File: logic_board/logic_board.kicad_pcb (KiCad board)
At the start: 4 copper layers, 80 x 30 mm, 61 parts, among them J1 SWD, J2 Audio In, J3 SJ2-3595X-SMT, J4 Amphenol 124015, J5 Batt, J6 Serial, SW1 TL3315NF160Q, SW2 TL3315NF160Q, SW3 TL3315NF160Q, SW4 TL3315NF160Q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

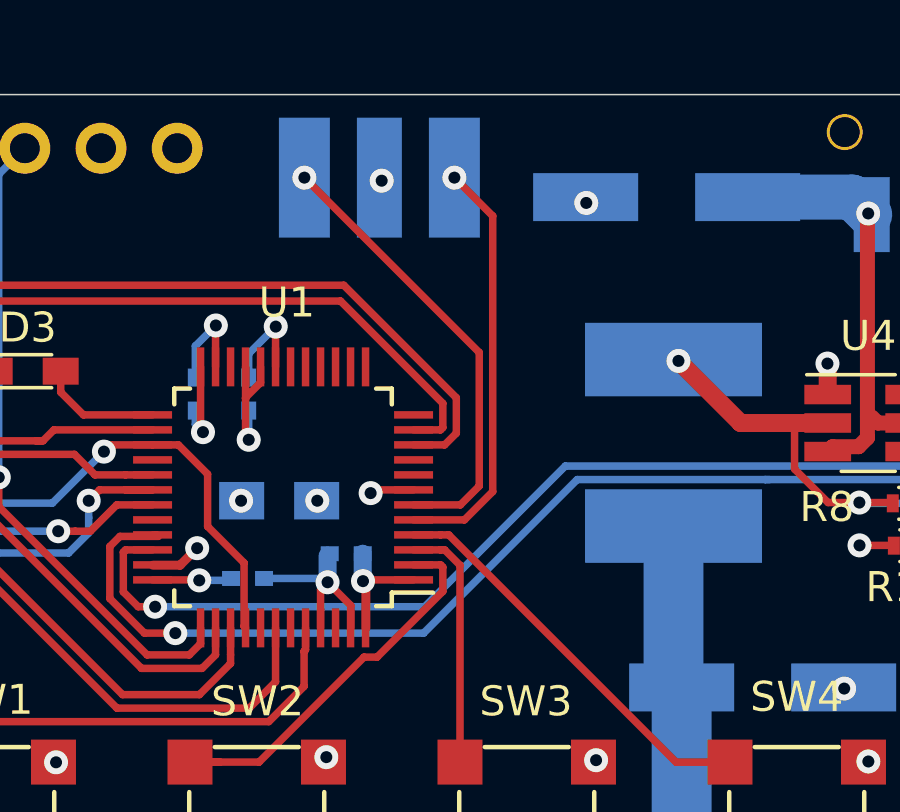
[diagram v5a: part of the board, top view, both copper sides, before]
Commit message: Move resonator closer to MCU.
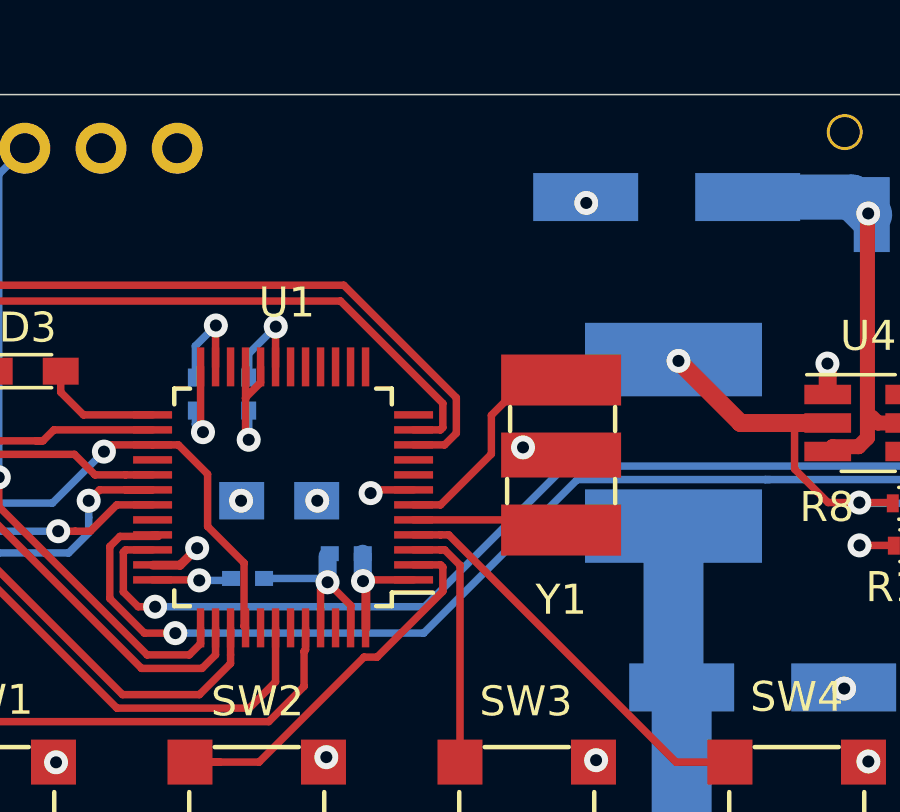
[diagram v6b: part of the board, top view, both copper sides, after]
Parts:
- Y1: moved to F.Cu
- moved Y1 11.1 mm to (152.1, 112.0), turned to 270 degrees
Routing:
- net Net-(U1-Pad5): track 14.0 -> 5.06 mm, vias 1 -> 0
- net Net-(U1-Pad6): track 15.1 -> 7.40 mm, vias 1 -> 0
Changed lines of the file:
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@@
     (thickness 1.6)
     (drawings 21)
-    (tracks 553)
+    (tracks 550)
     (zones 0)
     (modules 61)
@@
       (net 51 "Net-(U3-Pad26)"))
   )
-  (module custom_footprints:AWSCR-8.00CPLB-C30-T4 (layer B.Cu)
-    (at 146.0881 102.7684)
-    (fp_text reference Y1 (at -0.0381 3.6576) (layer B.SilkS)
-      (effects (font (size 1 1) (thickness 0.15)) (justify mirror))
-    )
-    (fp_text value "8 MHz" (at 1 5.6) (layer B.Fab)
-      (effects (font (size 1 1) (thickness 0.15)) (justify mirror))
-    )
-    (fp_line (start 0.8 -1.8) (end 1.6 -1.8) (layer B.SilkS) (width 0.15))
-    (fp_line (start 0.8 1.8) (end 1.6 1.8) (layer B.SilkS) (width 0.15))
-    (fp_line (start -0.8 -1.7) (end -1.6 -1.7) (layer B.SilkS) (width 0.15))
-    (fp_line (start -1.6 1.8) (end -0.8 1.8) (layer B.SilkS) (width 0.15))
-    (fp_line (start -4.2 -2.5) (end -4.2 2.5) (layer B.CrtYd) (width 0.12))
-    (fp_line (start -4.2 -2.5) (end 4.2 -2.5) (layer B.CrtYd) (width 0.12))
-    (fp_line (start 4.2 2.5) (end 4.2 -2.5) (layer B.CrtYd) (width 0.12))
-    (fp_line (start -4.2 2.5) (end 4.2 2.5) (layer B.CrtYd) (width 0.12))
-    (pad 3 smd rect (at 2.5 0) (size 1.7 4) (layers B.Cu B.Paste B.Mask)
+  (module custom_footprints:AWSCR-8.00CPLB-C30-T4 (layer F.Cu)
+    (at 152.146 112.014 270)
+    (fp_text reference Y1 (at 4.826 0) (layer F.SilkS)
+      (effects (font (size 1 1) (thickness 0.15)))
+    )
+    (fp_text value "8 MHz" (at 1 -5.6 270) (layer F.Fab)
+      (effects (font (size 1 1) (thickness 0.15)))
+    )
+    (fp_line (start 0.8 1.8) (end 1.6 1.8) (layer F.SilkS) (width 0.15))
+    (fp_line (start 0.8 -1.8) (end 1.6 -1.8) (layer F.SilkS) (width 0.15))
+    (fp_line (start -0.8 1.7) (end -1.6 1.7) (layer F.SilkS) (width 0.15))
+    (fp_line (start -1.6 -1.8) (end -0.8 -1.8) (layer F.SilkS) (width 0.15))
+    (fp_line (start -4.2 2.5) (end -4.2 -2.5) (layer F.CrtYd) (width 0.12))
+    (fp_line (start -4.2 2.5) (end 4.2 2.5) (layer F.CrtYd) (width 0.12))
+    (fp_line (start 4.2 -2.5) (end 4.2 2.5) (layer F.CrtYd) (width 0.12))
+    (fp_line (start -4.2 -2.5) (end 4.2 -2.5) (layer F.CrtYd) (width 0.12))
+    (pad 3 smd rect (at 2.5 0 270) (size 1.7 4) (layers F.Cu F.Paste F.Mask)
       (net 32 "Net-(U1-Pad5)"))
-    (pad 2 smd rect (at 0 0) (size 1.5 4) (layers B.Cu B.Paste B.Mask)
-      (net 2 GND))
-    (pad 1 smd rect (at -2.5 0) (size 1.7 4) (layers B.Cu B.Paste B.Mask)
+    (pad 2 smd rect (at 0 0 270) (size 1.5 4) (layers F.Cu F.Paste F.Mask)
+      (net 2 GND))
+    (pad 1 smd rect (at -2.5 0 270) (size 1.7 4) (layers F.Cu F.Paste F.Mask)
       (net 33 "Net-(U1-Pad6)"))
   )
@@
   (gr_line (start 180 102.5) (end 180 127.5) (layer Edge.Cuts) (width 0.05))
   (gr_line (start 102.5 100) (end 113 100) (layer Edge.Cuts) (width 0.05))
+  (via (at 150.876 111.76) (size 0.8) (drill 0.4) (layers F.Cu B.Cu) (net 2))
   (via (at 141.478 113.538) (size 0.8) (drill 0.4) (layers F.Cu B.Cu) (net 1))
   (via (at 156.17952 126.73076) (size 0.8) (drill 0.4) (layers F.Cu B.Cu) (net 1))
@@
   (via (at 166.37 128.7145) (size 0.8) (drill 0.4) (layers F.Cu B.Cu) (net 2))
   (via (at 152.9842 103.61168) (size 0.8) (drill 0.4) (layers F.Cu B.Cu) (net 2))
-  (via (at 146.1643 102.87) (size 0.8) (drill 0.4) (layers F.Cu B.Cu) (net 2))
   (via (at 160.6169 126.5301) (size 0.8) (drill 0.4) (layers F.Cu B.Cu) (net 2))
   (via (at 161.5821 119.7991) (size 0.8) (drill 0.4) (layers F.Cu B.Cu) (net 2))
@@
   (segment (start 172.7835 128.3407) (end 172.7907 128.3335) (width 0.25) (layer F.Cu) (net 31))
   (segment (start 172.7835 129.3114) (end 172.7835 128.3407) (width 0.25) (layer F.Cu) (net 31))
-  (via (at 148.5881 102.7684) (size 0.8) (drill 0.4) (layers F.Cu B.Cu) (net 32))
-  (segment (start 149.866611 104.046911) (end 148.5881 102.7684) (width 0.25) (layer F.Cu) (net 32))
-  (segment (start 149.866611 113.234201) (end 149.866611 104.046911) (width 0.25) (layer F.Cu) (net 32))
-  (segment (start 148.924572 114.17624) (end 149.866611 113.234201) (width 0.25) (layer F.Cu) (net 32))
-  (segment (start 147.22754 114.17624) (end 148.924572 114.17624) (width 0.25) (layer F.Cu) (net 32))
-  (segment (start 149.416601 108.596901) (end 143.5881 102.7684) (width 0.25) (layer F.Cu) (net 33))
-  (via (at 143.5881 102.7684) (size 0.8) (drill 0.4) (layers F.Cu B.Cu) (net 33))
-  (segment (start 148.788162 113.67624) (end 149.416601 113.047801) (width 0.25) (layer F.Cu) (net 33))
-  (segment (start 149.416601 113.047801) (end 149.416601 108.596901) (width 0.25) (layer F.Cu) (net 33))
-  (segment (start 147.22754 113.67624) (end 148.788162 113.67624) (width 0.25) (layer F.Cu) (net 33))
+  (segment (start 151.80824 114.17624) (end 152.146 114.514) (width 0.25) (layer F.Cu) (net 32))
+  (segment (start 147.22754 114.17624) (end 151.80824 114.17624) (width 0.25) (layer F.Cu) (net 32))
+  (segment (start 150.996 109.514) (end 152.146 109.514) (width 0.25) (layer F.Cu) (net 33))
+  (segment (start 149.820999 110.689001) (end 150.996 109.514) (width 0.25) (layer F.Cu) (net 33))
+  (segment (start 149.820999 111.982781) (end 149.820999 110.689001) (width 0.25) (layer F.Cu) (net 33))
+  (segment (start 148.12754 113.67624) (end 149.820999 111.982781) (width 0.25) (layer F.Cu) (net 33))
+  (segment (start 147.22754 113.67624) (end 148.12754 113.67624) (width 0.25) (layer F.Cu) (net 33))
   (segment (start 114.398372 117.387396) (end 120.24406 111.54171) (width 0.25) (layer F.Cu) (net 40))
   (segment (start 114.398371 120.906571) (end 114.398372 117.387396) (width 0.25) (layer F.Cu) (net 40))

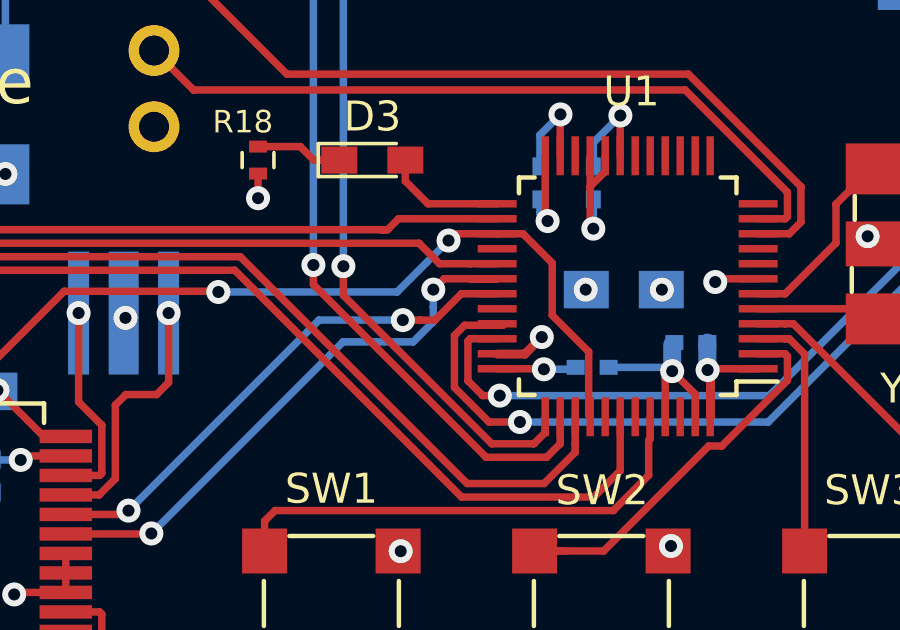
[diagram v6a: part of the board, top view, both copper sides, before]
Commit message: Move I2C2_SDA from PA8 to PA10
There is conflicting information in the datahsheet. Table 13 says this
should be PA10, but Table 12 says PA8. I'm using the former, as it
has actual mappings. This would be fairly easy to rework with a blue
wire if I guessed wrong: jumpering the pins together and making PA10
be an input.
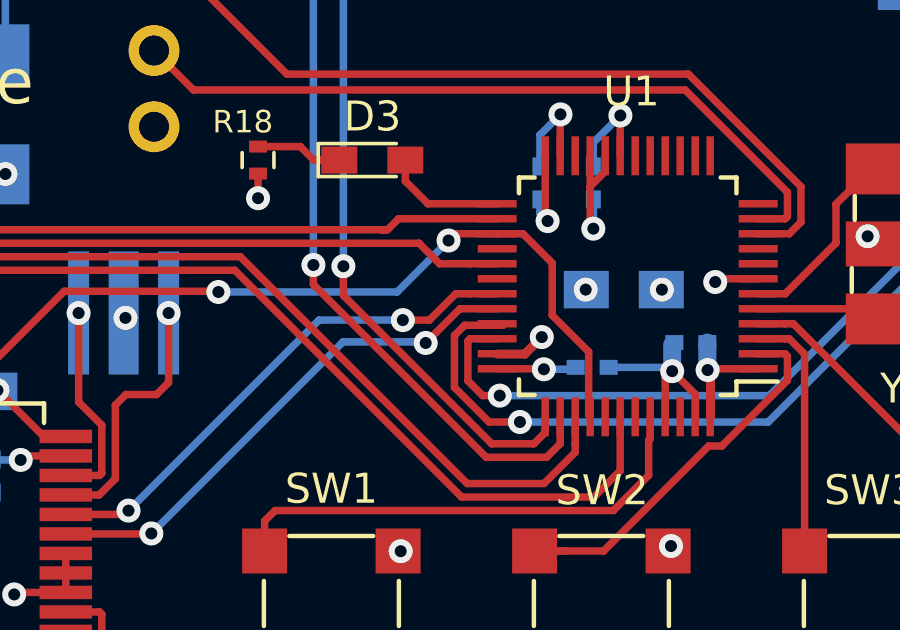
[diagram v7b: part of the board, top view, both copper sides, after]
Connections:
- U1 pad 30: SDA -> Net-(U1-Pad30)
- U1 pad 32: Net-(U1-Pad32) -> SDA
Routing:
- net SDA: track 19.4 -> 17.5 mm

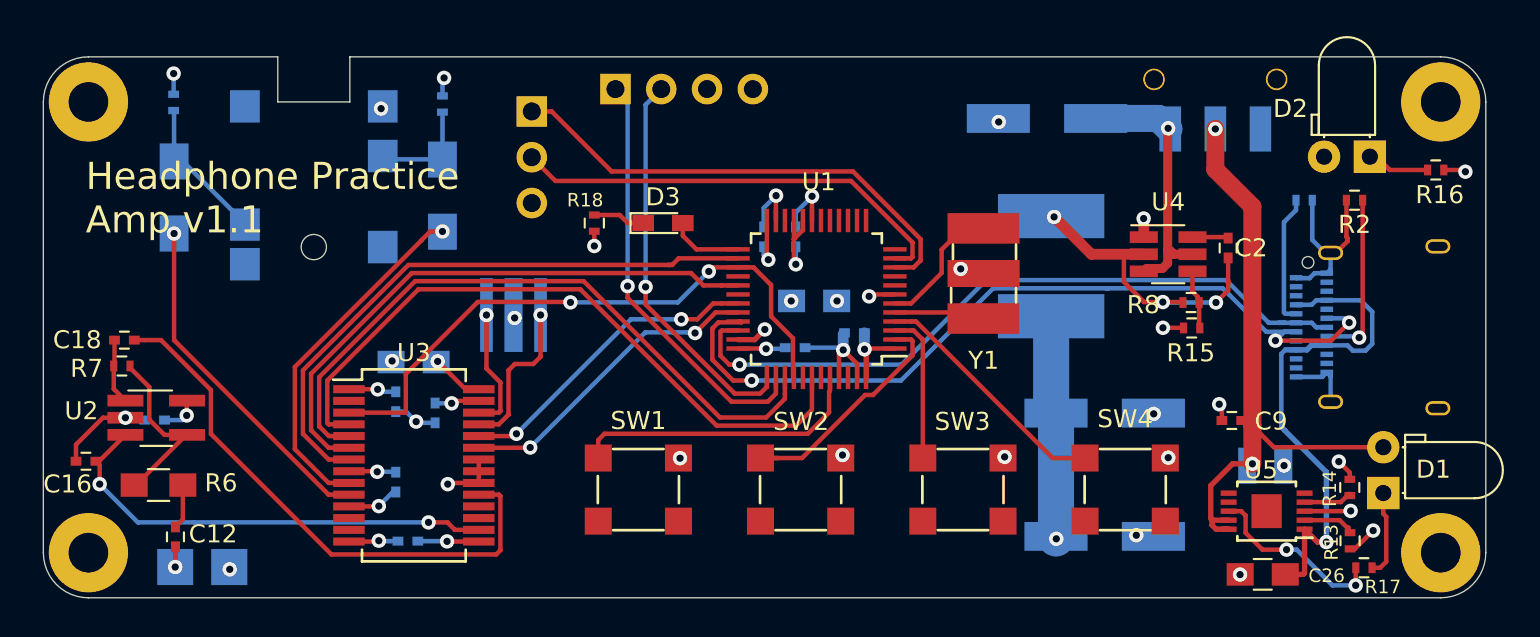
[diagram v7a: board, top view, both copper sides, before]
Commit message: Switch from switching to LDO regulator
This simplifies the design and reduces part count. Since the typical
use case is only a few hours of usage, the difference in efficiency
doesn't seem to justify the additional complexity.
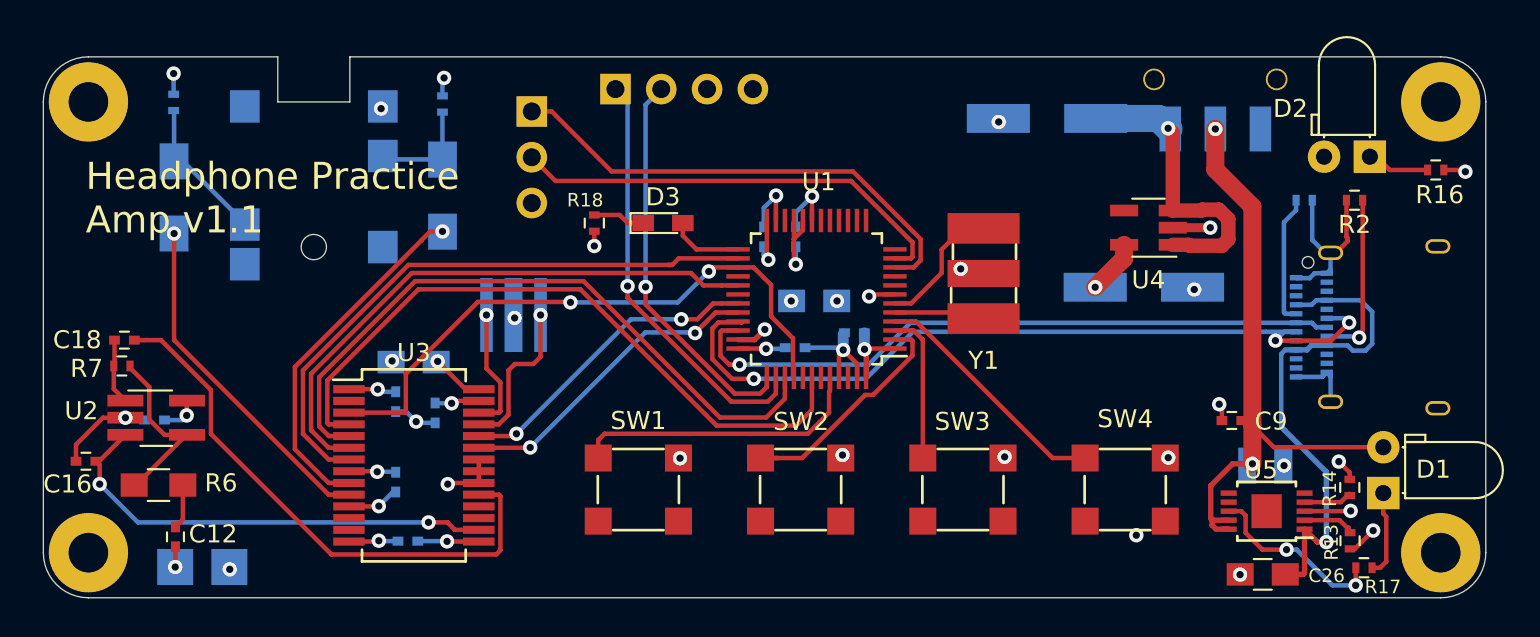
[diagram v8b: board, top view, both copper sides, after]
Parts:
- removed C1: 22uF, Capacitors_SMD:CP_Elec_6.3x4.5
- removed C2: 0.1uF, Capacitors_SMD:C_0402
- removed L1: 3.3 uH, Inductors_SMD:L_Taiyo-Yuden_NR-60xx_HandSoldering
- removed R15: 10k, Resistors_SMD:R_0402
- removed R8: 33.2k, Resistors_SMD:R_0402
- U4: value TPS562200 -> SPX3819M5-L-3-3; footprint TO_SOT_Packages_SMD:SOT-23-6_Handsoldering -> TO_SOT_Packages_SMD:SOT-23-5_HandSoldering
- moved C3 14.0 mm to (161.0, 112.8)
- moved U4 1.83 mm to (161.3, 109.5), turned to 180 degrees
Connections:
- U4 pad 1: GND -> Net-(C25-Pad1)
- U4 pad 2: Net-(C2-Pad2) -> GND
- U4 pad 5: Net-(C25-Pad1) -> +3V3
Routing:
- net Net-(C2-Pad2): track 18.0 -> 0.00 mm, vias 3 -> 0
- net +3V3: track 41.2 -> 31.8 mm
- net Net-(U4-Pad4): track 3.31 -> 0.00 mm
- net USB_DM: track 47.2 -> 44.7 mm
- net USB_DP: track 39.6 -> 37.2 mm
- net Net-(C25-Pad1): track 14.7 -> 16.7 mm
- net Net-(C2-Pad1): track 2.00 -> 0.00 mm
- net GND: track 61.9 -> 61.8 mm, vias 34 -> 33
